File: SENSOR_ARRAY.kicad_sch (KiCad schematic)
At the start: 44 parts, among them J2 FH34SRJ-8S-0.5SH_50_, Q1 MMBT3904, U10 QRE1113GR, U11 QRE1113GR, U12 QRE1113GR, U13 QRE1113GR, U14 QRE1113GR, U15 QRE1113GR, U16 QRE1113GR, U17 QRE1113GR, U18 QRE1113GR, U19 QRE1113GR, U20 QRE1113GR, U21 QRE1113GR, U6 QRE1113GR, U7 QRE1113GR, U8 QRE1113GR, U9 QRE1113GR

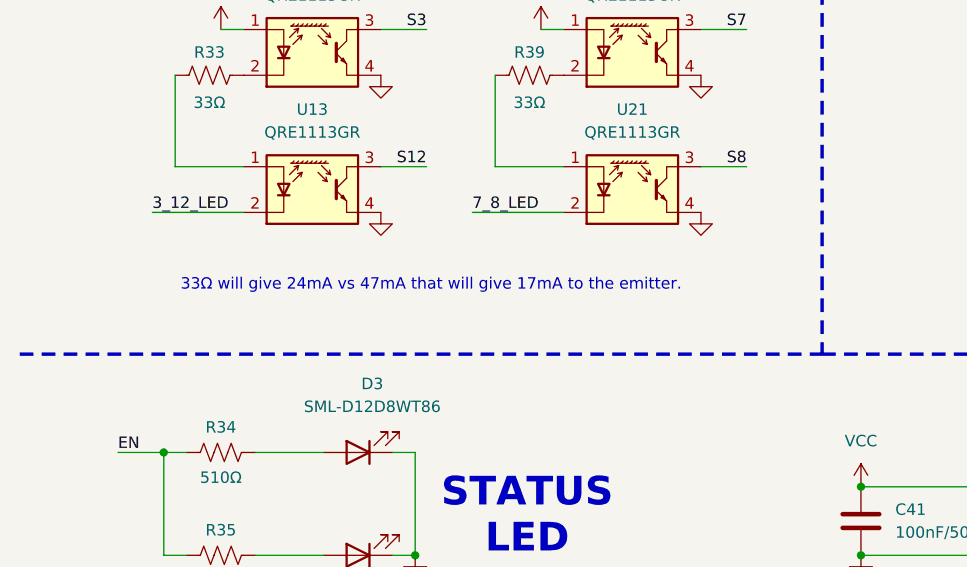
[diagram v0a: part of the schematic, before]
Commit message: Add SAMD51 pin planner and LFR torque calculator tools
Move samd51-pin-planner.html into Tools/ alongside a new
lfr-torque-calculator.html and its SAMD51A19J.json pin/peripheral
data source. Also ignore KiCad's transient *.lck files going forward.

Minor schematic touch-ups: corrected a resistor value typo in
SENSOR_ARRAY (47Ω, was mislabeled Ω-less) and updated the MCU
checklist note to reflect open questions (peripheral mux, current
sensing) instead of a stale done item.

Co-Authored-By: Claude Sonnet 5 <noreply@anthropic.com>
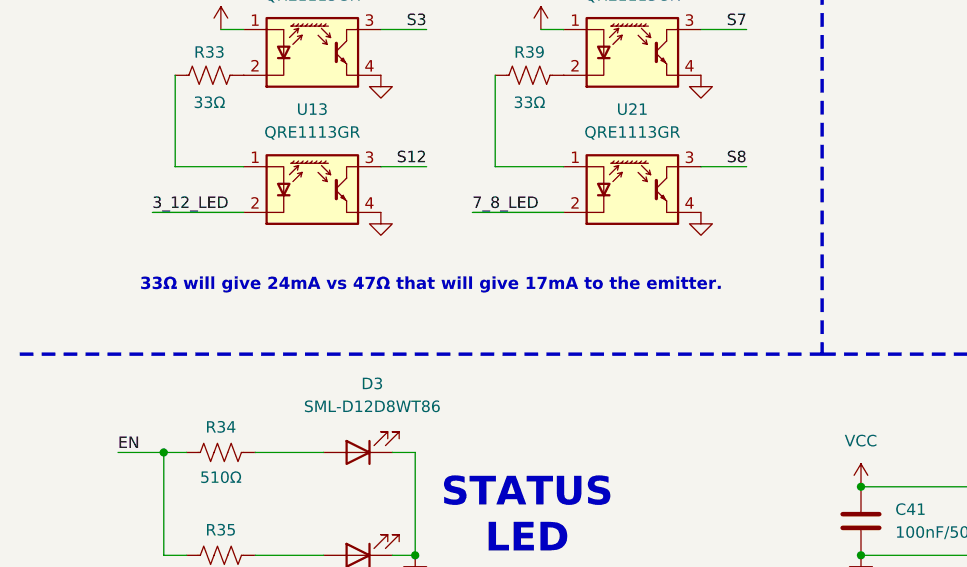
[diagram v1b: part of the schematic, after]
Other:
- note added: "33Ω will give 24mA vs 47Ω that will give 17mA to the emitter."
- note removed: "33Ω will give 24mA vs 47mA that will give 17mA to the emitter."
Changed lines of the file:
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@@
 		)
 	)
-	(text "33Ω will give 24mA vs 47mA that will give 17mA to the emitter."
+	(text "33Ω will give 24mA vs 47Ω that will give 17mA to the emitter."
 		(exclude_from_sim no)
 		(at 57.658 159.258 0)
 		(effects
 			(font
-				(size 1.27 1.27)
+				(size 1.35 1.35)
+				(thickness 0.27)
+				(bold yes)
 			)
 		)
